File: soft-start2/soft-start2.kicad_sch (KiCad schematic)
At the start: 58 parts, among them J10 Conn_01x02_Pin, J11 Conn_01x02_Socket, J3 Conn_01x01_Pin, J4 Conn_01x01_Pin, J5 Conn_01x01_Pin, J8 Conn_01x01_Pin, K1 Relay_SPST-NO, K2 Relay_SPST-NO, M1 Motor_DC, Q1 IRFB3004PbF, Q2 IRFB3004PbF, SW1 SW_SPST_Temperature, U1 P0102BL, U2 TLC555xD, U3 TS391ILT, U4 IRS10752LPbF, U5 4011

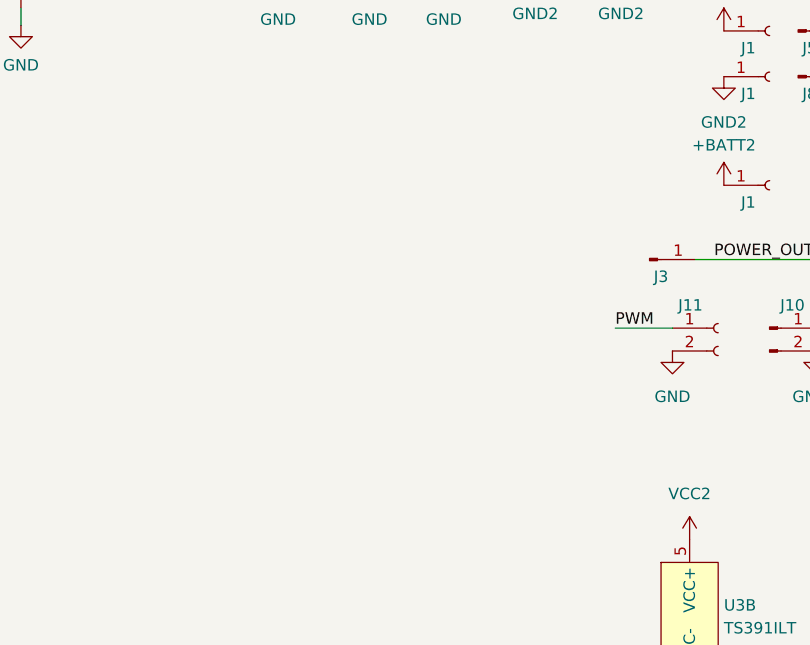
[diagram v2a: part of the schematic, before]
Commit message: [soft-start] Complete basic PCB for PWM soft-start
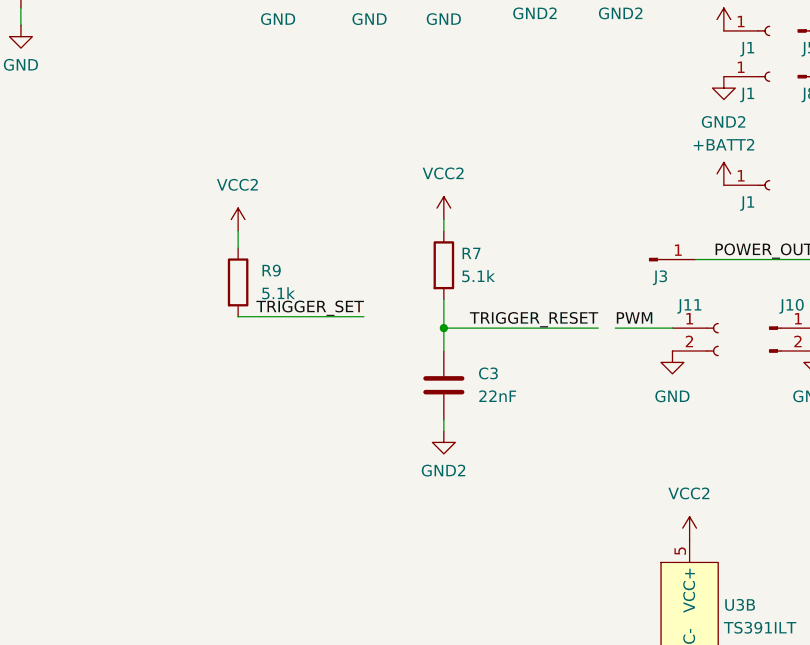
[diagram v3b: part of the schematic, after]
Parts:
- added C3: 22nF, Capacitor_THT:C_Disc_D5.0mm_W2.5mm_P5.00mm, symbol Device:C
- added R7: 5.1k, Resistor_THT:R_Axial_DIN0207_L6.3mm_D2.5mm_P7.62mm_Horizontal, symbol Device:R
- added R9: 5.1k, Resistor_THT:R_Axial_DIN0204_L3.6mm_D1.6mm_P5.08mm_Horizontal, symbol Device:R
- C2, C6: footprint Capacitor_THT:C_Disc_D6.0mm_W4.4mm_P5.00mm -> Capacitor_THT:C_Disc_D5.0mm_W2.5mm_P5.00mm
- C5: footprint Capacitor_THT:C_Disc_D5.0mm_W2.5mm_P5.00mm -> Capacitor_THT:C_Disc_D7.5mm_W5.0mm_P7.50mm
- R8: footprint Resistor_THT:R_Axial_DIN0207_L6.3mm_D2.5mm_P5.08mm_Vertical -> Resistor_THT:R_Axial_DIN0207_L6.3mm_D2.5mm_P10.16mm_Horizontal
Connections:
- net GND2: now also C3.2
- net TRIGGER_RESET: now also C3.1, R7.2
- net TRIGGER_SET: now also R9.2
- net VCC2: now also R7.1, R9.1
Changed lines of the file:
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@@
   (junction (at 140.335 173.355) (diameter 0) (color 0 0 0 0)
   )
+  (junction (at 236.855 67.945) (diameter 0) (color 0 0 0 0)
+  )
   (junction (at 67.31 62.23) (diameter 0) (color 0 0 0 0)
   )
@@
     (stroke (width 0) (type default))
   )
+  (wire (pts (xy 213.995 66.675) (xy 227.965 66.675))
+    (stroke (width 0) (type default))
+  )
   (wire (pts (xy 48.895 77.47) (xy 59.69 77.47))
     (stroke (width 0) (type default))
@@
     (stroke (width 0) (type default))
   )
+  (wire (pts (xy 236.855 67.945) (xy 254 67.945))
+    (stroke (width 0) (type default))
+  )
   (wire (pts (xy 17.145 87.63) (xy 24.13 87.63))
     (stroke (width 0) (type default))
@@
     (stroke (width 0) (type default))
   )
+  (wire (pts (xy 236.855 55.88) (xy 236.855 57.15))
+    (stroke (width 0) (type default))
+  )
   (wire (pts (xy 24.765 166.37) (xy 24.765 167.64))
     (stroke (width 0) (type default))
@@
     (stroke (width 0) (type default))
   )
+  (wire (pts (xy 236.855 67.945) (xy 236.855 70.485))
+    (stroke (width 0) (type default))
+  )
   (wire (pts (xy 24.765 149.225) (xy 30.48 149.225))
     (stroke (width 0) (type default))
@@
     (stroke (width 0) (type default))
   )
+  (wire (pts (xy 236.855 64.77) (xy 236.855 67.945))
+    (stroke (width 0) (type default))
+  )
   (wire (pts (xy 23.495 43.18) (xy 41.275 43.18))
     (stroke (width 0) (type default))
@@
     (stroke (width 0) (type default))
   )
+  (wire (pts (xy 213.995 57.15) (xy 213.995 59.055))
+    (stroke (width 0) (type default))
+  )
   (wire (pts (xy 150.495 62.23) (xy 164.465 62.23))
     (stroke (width 0) (type default))
@@
     (stroke (width 0) (type default))
   )
+  (wire (pts (xy 236.855 78.105) (xy 236.855 79.375))
+    (stroke (width 0) (type default))
+  )
   (wire (pts (xy 140.335 183.515) (xy 140.335 185.42))
     (stroke (width 0) (type default))
@@
     (effects (font (size 1.27 1.27)) (justify right bottom))
   )
+  (label "TRIGGER_SET" (at 227.965 66.675 180) (fields_autoplaced)
+    (effects (font (size 1.27 1.27)) (justify right bottom))
+  )
   (label "TRIGGER_OUT" (at 109.855 178.435 0) (fields_autoplaced)
     (effects (font (size 1.27 1.27)) (justify left bottom))
@@
     (effects (font (size 1.27 1.27)) (justify right bottom))
   )
+  (label "TRIGGER_RESET" (at 254 67.945 180) (fields_autoplaced)
+    (effects (font (size 1.27 1.27)) (justify right bottom))
+  )
   (symbol (lib_id "power:+BATT") (at 171.45 20.955 0) (unit 1)
     (in_bom yes) (on_board yes) (dnp no) (fields_autoplaced)
@@
     )
   )
+  (symbol (lib_id "Device:C") (at 236.855 74.295 0) (unit 1)
+    (in_bom yes) (on_board yes) (dnp no) (fields_autoplaced)
+    (property "Reference" "C3" (at 240.665 73.025 0)
+      (effects (font (size 1.27 1.27)) (justify left))
+    )
+    (property "Value" "22nF" (at 240.665 75.565 0)
+      (effects (font (size 1.27 1.27)) (justify left))
+    )
+    (property "Footprint" "Capacitor_THT:C_Disc_D5.0mm_W2.5mm_P5.00mm" (at 237.8202 78.105 0)
+      (effects (font (size 1.27 1.27)) hide)
+    )
+    (property "Datasheet" "~" (at 236.855 74.295 0)
+      (effects (font (size 1.27 1.27)) hide)
+    )
+    (pin "1")
+    (pin "2")
+    (instances
+      (project "soft-start"
+        (path "/dd3da890-32ef-4a5a-aea4-e5d2141f1ff1"
+          (reference "C3") (unit 1)
+        )
+      )
+      (project "soft-start2"
+        (path "/ebfa1560-6bfd-4c13-8584-dcc8e4637497"
+          (reference "C14") (unit 1)
+        )
+      )
+    )
+  )
   (symbol (lib_id "Device:R") (at 23.495 111.125 0) (unit 1)
     (in_bom yes) (on_board yes) (dnp no) (fields_autoplaced)
@@
       (effects (font (size 1.27 1.27)) (justify left))
     )
-    (property "Footprint" "Resistor_THT:R_Axial_DIN0207_L6.3mm_D2.5mm_P5.08mm_Vertical" (at 21.717 111.125 90)
+    (property "Footprint" "Resistor_THT:R_Axial_DIN0207_L6.3mm_D2.5mm_P10.16mm_Horizontal" (at 21.717 111.125 90)
       (effects (font (size 1.27 1.27)) hide)
     )
@@
     )
   )
+  (symbol (lib_id "Device:R") (at 236.855 60.96 0) (unit 1)
+    (in_bom yes) (on_board yes) (dnp no) (fields_autoplaced)
+    (property "Reference" "R7" (at 238.76 59.69 0)
+      (effects (font (size 1.27 1.27)) (justify left))
+    )
+    (property "Value" "5.1k" (at 238.76 62.23 0)
+      (effects (font (size 1.27 1.27)) (justify left))
+    )
+    (property "Footprint" "Resistor_THT:R_Axial_DIN0207_L6.3mm_D2.5mm_P7.62mm_Horizontal" (at 235.077 60.96 90)
+      (effects (font (size 1.27 1.27)) hide)
+    )
+    (property "Datasheet" "~" (at 236.855 60.96 0)
+      (effects (font (size 1.27 1.27)) hide)
+    )
+    (pin "1")
+    (pin "2")
+    (instances
+      (project "soft-start"
+        (path "/dd3da890-32ef-4a5a-aea4-e5d2141f1ff1"
+          (reference "R7") (unit 1)
+        )
+      )
+      (project "soft-start2"
+        (path "/ebfa1560-6bfd-4c13-8584-dcc8e4637497"
+          (reference "R10") (unit 1)
+        )
+      )
+    )
+  )
   (symbol (lib_id "power:GND2") (at 278.13 70.485 0) (unit 1)
     (in_bom yes) (on_board yes) (dnp no) (fields_autoplaced)
@@
     )
   )
+  (symbol (lib_id "vcc2:VCC2") (at 236.855 55.88 0) (unit 1)
+    (in_bom yes) (on_board yes) (dnp no) (fields_autoplaced)
+    (property "Reference" "#PWR053" (at 236.855 59.69 0)
+      (effects (font (size 1.27 1.27)) hide)
+    )
+    (property "Value" "VCC2" (at 236.855 50.8 0)
+      (effects (font (size 1.27 1.27)))
+    )
+    (property "Footprint" "" (at 236.855 55.88 0)
+      (effects (font (size 1.27 1.27)) hide)
+    )
+    (property "Datasheet" "" (at 236.855 55.88 0)
+      (effects (font (size 1.27 1.27)) hide)
+    )
+    (pin "1")
+    (instances
+      (project "soft-start2"
+        (path "/ebfa1560-6bfd-4c13-8584-dcc8e4637497"
+          (reference "#PWR053") (unit 1)
+        )
+      )
+    )
+  )
   (symbol (lib_id "Device:C") (at 118.745 50.8 0) (mirror y) (unit 1)
     (in_bom yes) (on_board yes) (dnp no) (fields_autoplaced)
@@
     )
   )
+  (symbol (lib_id "Device:R") (at 213.995 62.865 0) (unit 1)
+    (in_bom yes) (on_board yes) (dnp no) (fields_autoplaced)
+    (property "Reference" "R9" (at 216.535 61.595 0)
+      (effects (font (size 1.27 1.27)) (justify left))
+    )
+    (property "Value" "5.1k" (at 216.535 64.135 0)
+      (effects (font (size 1.27 1.27)) (justify left))
+    )
+    (property "Footprint" "Resistor_THT:R_Axial_DIN0204_L3.6mm_D1.6mm_P5.08mm_Horizontal" (at 212.217 62.865 90)
+      (effects (font (size 1.27 1.27)) hide)
+    )
+    (property "Datasheet" "~" (at 213.995 62.865 0)
+      (effects (font (size 1.27 1.27)) hide)
+    )
+    (pin "1")
+    (pin "2")
+    (instances
+      (project "soft-start"
+        (path "/dd3da890-32ef-4a5a-aea4-e5d2141f1ff1"
+          (reference "R9") (unit 1)
+        )
+      )
+      (project "soft-start2"
+        (path "/ebfa1560-6bfd-4c13-8584-dcc8e4637497"
+          (reference "R11") (unit 1)
+        )
+      )
+    )
+  )
   (symbol (lib_id "Device:C") (at 160.02 139.7 0) (unit 1)
     (in_bom yes) (on_board yes) (dnp no) (fields_autoplaced)
@@
       (effects (font (size 1.27 1.27)) (justify left))
     )
-    (property "Footprint" "Capacitor_THT:C_Disc_D6.0mm_W4.4mm_P5.00mm" (at 160.9852 143.51 0)
+    (property "Footprint" "Capacitor_THT:C_Disc_D5.0mm_W2.5mm_P5.00mm" (at 160.9852 143.51 0)
       (effects (font (size 1.27 1.27)) hide)
     )
@@
     )
   )
+  (symbol (lib_id "vcc2:VCC2") (at 213.995 57.15 0) (unit 1)
+    (in_bom yes) (on_board yes) (dnp no) (fields_autoplaced)
+    (property "Reference" "#PWR054" (at 213.995 60.96 0)
+      (effects (font (size 1.27 1.27)) hide)
+    )
+    (property "Value" "VCC2" (at 213.995 52.07 0)
+      (effects (font (size 1.27 1.27)))
+    )
+    (property "Footprint" "" (at 213.995 57.15 0)
+      (effects (font (size 1.27 1.27)) hide)
+    )
+    (property "Datasheet" "" (at 213.995 57.15 0)
+      (effects (font (size 1.27 1.27)) hide)
+    )
+    (pin "1")
+    (instances
+      (project "soft-start2"
+        (path "/ebfa1560-6bfd-4c13-8584-dcc8e4637497"
+          (reference "#PWR054") (unit 1)
+        )
+      )
+    )
+  )
   (symbol (lib_id "Device:C") (at 46.99 72.39 90) (unit 1)
     (in_bom yes) (on_board yes) (dnp no) (fields_autoplaced)
@@
       (effects (font (size 1.27 1.27)) (justify left))
     )
-    (property "Footprint" "Capacitor_THT:C_Disc_D6.0mm_W4.4mm_P5.00mm" (at 160.9852 116.84 0)
+    (property "Footprint" "Capacitor_THT:C_Disc_D5.0mm_W2.5mm_P5.00mm" (at 160.9852 116.84 0)
       (effects (font (size 1.27 1.27)) hide)
     )
@@
       (effects (font (size 1.27 1.27)) (justify left))
     )
-    (property "Footprint" "Capacitor_THT:C_Disc_D5.0mm_W2.5mm_P5.00mm" (at 257.5052 28.575 0)
+    (property "Footprint" "Capacitor_THT:C_Disc_D7.5mm_W5.0mm_P7.50mm" (at 257.5052 28.575 0)
       (effects (font (size 1.27 1.27)) hide)
     )
@@
         )
       )
+    )
+  )
+  (symbol (lib_id "power:GND2") (at 236.855 79.375 0) (unit 1)
+    (in_bom yes) (on_board yes) (dnp no) (fields_autoplaced)
+    (property "Reference" "#PWR052" (at 236.855 85.725 0)
+      (effects (font (size 1.27 1.27)) hide)
+    )
+    (property "Value" "GND2" (at 236.855 83.82 0)
+      (effects (font (size 1.27 1.27)))
+    )
+    (property "Footprint" "" (at 236.855 79.375 0)
+      (effects (font (size 1.27 1.27)) hide)
+    )
+    (property "Datasheet" "" (at 236.855 79.375 0)
+      (effects (font (size 1.27 1.27)) hide)
+    )
+    (pin "1")
+    (instances
+      (project "soft-start2"
+        (path "/ebfa1560-6bfd-4c13-8584-dcc8e4637497"
+          (reference "#PWR052") (unit 1)
+        )
+      )

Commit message: [soft-start] Reset PWM generator on trigger latch. Update plot settings
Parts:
- added J12: Conn_01x01_Pin, Connector_Wire:SolderWire-0.5sqmm_1x01_D0.9mm_OD2.1mm, symbol Connector:Conn_01x01_Pin
- added J13: Conn_01x01_Socket, Connector_Wire:SolderWire-0.5sqmm_1x01_D0.9mm_OD2.1mm, symbol Connector:Conn_01x01_Socket
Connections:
- net VCC: no longer U2.4 (R)
- net TRIGGER_OUT_INV: now reaches C2.1, Rt2.1, U1.12
- net TRIGGER_OUT_INV: now also J12.1 (Pin_1)
- new net: J13.1 (Pin_1), U2.4 (R)
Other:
- note added: "Connections: J12 -> J13 J11 -> J10 J5 -> J6 J7 -> J8 J3 - controlled cooling fan J1 - external battery +12V J2 - external GND J9 - external battery +12V L1 is an external relay capable of driving M1's full power current (approx. 30 amps)"
- note removed: "L1 is an external relay capable of driving M1's full power current (approx. 30 amps)"
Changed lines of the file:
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@@
   (junction (at 153.67 135.89) (diameter 0) (color 0 0 0 0)
   )
+  (junction (at 160.02 135.89) (diameter 0) (color 0 0 0 0)
+  )
   (junction (at 142.875 173.355) (diameter 0) (color 0 0 0 0)
   )
@@
     (stroke (width 0) (type default))
   )
-  (wire (pts (xy 23.495 43.18) (xy 41.275 43.18))
-    (stroke (width 0) (type default))
-  )
   (wire (pts (xy 167.005 83.82) (xy 179.705 83.82))
     (stroke (width 0) (type default))
@@
     (stroke (width 0) (type default))
   )
+  (wire (pts (xy 31.75 43.18) (xy 41.275 43.18))
+    (stroke (width 0) (type default))
+  )
   (wire (pts (xy 66.675 38.1) (xy 75.565 38.1))
     (stroke (width 0) (type default))
@@
     (stroke (width 0) (type default))
   )
+  (wire (pts (xy 160.02 135.89) (xy 171.45 135.89))
+    (stroke (width 0) (type default))
+  )
   (wire (pts (xy 29.845 60.96) (xy 33.655 60.96))
     (stroke (width 0) (type default))
@@
     (effects (font (size 1.27 1.27)) (justify left bottom))
   )
-  (text "L1 is an external relay capable of driving M1's full power current (approx. 30 amps)\n"
+  (text "Connections:\nJ12 -> J13\nJ11 -> J10\nJ5 -> J6\nJ7 -> J8\n\nJ3 - controlled cooling fan\nJ1 - external battery +12V\nJ2 - external GND\nJ9 - external battery +12V\n\nL1 is an external relay capable of driving M1's full power current (approx. 30 amps)"
     (at 182.88 162.56 0)
     (effects (font (size 1.27 1.27)) (justify left bottom))
@@
     (effects (font (size 1.27 1.27)) (justify right bottom))
   )
+  (label "TRIGGER_OUT_INV" (at 171.45 135.89 180) (fields_autoplaced)
+    (effects (font (size 1.27 1.27)) (justify right bottom))
+  )
   (label "PWM2" (at 283.21 67.945 180) (fields_autoplaced)
     (effects (font (size 1.27 1.27)) (justify right bottom))
@@
     )
   )
-  (symbol (lib_id "power:VCC") (at 23.495 43.18 0) (unit 1)
-    (in_bom yes) (on_board yes) (dnp no) (fields_autoplaced)
-    (property "Reference" "#PWR018" (at 23.495 46.99 0)
-      (effects (font (size 1.27 1.27)) hide)
-    )
-    (property "Value" "VCC" (at 23.495 38.1 0)
-      (effects (font (size 1.27 1.27)))
-    )
-    (property "Footprint" "" (at 23.495 43.18 0)
-      (effects (font (size 1.27 1.27)) hide)
-    )
-    (property "Datasheet" "" (at 23.495 43.18 0)
-      (effects (font (size 1.27 1.27)) hide)
-    )
-    (pin "1")
-    (instances
-      (project "soft-start2"
-        (path "/ebfa1560-6bfd-4c13-8584-dcc8e4637497"
-          (reference "#PWR018") (unit 1)
-        )
-      )
-    )
-  )
   (symbol (lib_id "vcc2:VCC2") (at 267.97 34.925 0) (unit 1)
     (in_bom yes) (on_board yes) (dnp no) (fields_autoplaced)
@@
     )
   )
+  (symbol (lib_id "Connector:Conn_01x01_Pin") (at 176.53 135.89 180) (unit 1)
+    (in_bom yes) (on_board yes) (dnp no) (fields_autoplaced)
+    (property "Reference" "J12" (at 175.895 130.81 0)
+      (effects (font (size 1.27 1.27)))
+    )
+    (property "Value" "Conn_01x01_Pin" (at 175.895 133.35 0)
+      (effects (font (size 1.27 1.27)) hide)
+    )
+    (property "Footprint" "Connector_Wire:SolderWire-0.5sqmm_1x01_D0.9mm_OD2.1mm" (at 176.53 135.89 0)
+      (effects (font (size 1.27 1.27)) hide)
+    )
+    (property "Datasheet" "~" (at 176.53 135.89 0)
+      (effects (font (size 1.27 1.27)) hide)
+    )
+    (pin "1")
+    (instances
+      (project "soft-start2"
+        (path "/ebfa1560-6bfd-4c13-8584-dcc8e4637497"
+          (reference "J12") (unit 1)
+        )
+      )
+    )
+  )
   (symbol (lib_id "power:GND") (at 53.975 48.26 0) (unit 1)
     (in_bom yes) (on_board yes) (dnp no) (fields_autoplaced)
@@
         )
       )
+    )
+  )
+  (symbol (lib_id "Connector:Conn_01x01_Socket") (at 26.67 43.18 180) (unit 1)
+    (in_bom yes) (on_board yes) (dnp no) (fields_autoplaced)
+    (property "Reference" "J13" (at 27.305 38.1 0)
+      (effects (font (size 1.27 1.27)))
+    )
+    (property "Value" "Conn_01x01_Socket" (at 27.305 40.64 0)
+      (effects (font (size 1.27 1.27)) hide)
+    )
+    (property "Footprint" "Connector_Wire:SolderWire-0.5sqmm_1x01_D0.9mm_OD2.1mm" (at 26.67 43.18 0)
+      (effects (font (size 1.27 1.27)) hide)
+    )
+    (property "Datasheet" "~" (at 26.67 43.18 0)
+      (effects (font (size 1.27 1.27)) hide)
+    )
+    (pin "1")
+    (instances
+      (project "soft-start2"
+        (path "/ebfa1560-6bfd-4c13-8584-dcc8e4637497"
+          (reference "J13") (unit 1)
+        )
+      )

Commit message: [soft-start] Add capacitor discharge resistor. It limits capacitor voltage to approx. 90% of VCC
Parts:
- added R12: 24k, Resistor_THT:R_Axial_DIN0207_L6.3mm_D2.5mm_P7.62mm_Horizontal, symbol Device:R
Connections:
- net GND: now also R12.2
- net U1_CONT: now also R12.1
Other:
- moved on the sheet: J12
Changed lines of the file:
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@@
   (junction (at 150.495 62.23) (diameter 0) (color 0 0 0 0)
   )
+  (junction (at 164.465 53.34) (diameter 0) (color 0 0 0 0)
+  )
   (junction (at 140.335 160.02) (diameter 0) (color 0 0 0 0)
   )
@@
   )
   (junction (at 160.02 135.89) (diameter 0) (color 0 0 0 0)
+  )
+  (junction (at 164.465 62.23) (diameter 0) (color 0 0 0 0)
   )
   (junction (at 142.875 173.355) (diameter 0) (color 0 0 0 0)
@@
     (stroke (width 0) (type default))
   )
+  (wire (pts (xy 180.975 62.23) (xy 180.975 61.595))
+    (stroke (width 0) (type default))
+  )
   (wire (pts (xy 150.495 22.86) (xy 150.495 26.035))
     (stroke (width 0) (type default))
@@
     (stroke (width 0) (type default))
   )
+  (wire (pts (xy 153.67 151.765) (xy 153.67 135.89))
+    (stroke (width 0) (type default))
+  )
   (wire (pts (xy 140.335 185.42) (xy 140.335 189.23))
     (stroke (width 0) (type default))
@@
     (stroke (width 0) (type default))
   )
+  (wire (pts (xy 164.465 62.23) (xy 180.975 62.23))
+    (stroke (width 0) (type default))
+  )
   (wire (pts (xy 67.945 109.22) (xy 69.85 109.22))
     (stroke (width 0) (type default))
@@
     (stroke (width 0) (type default))
   )
+  (wire (pts (xy 180.975 53.34) (xy 164.465 53.34))
+    (stroke (width 0) (type default))
+  )
   (wire (pts (xy 189.865 32.385) (xy 189.865 34.29))
     (stroke (width 0) (type default))
@@
     (stroke (width 0) (type default))
   )
+  (wire (pts (xy 156.845 151.765) (xy 153.67 151.765))
+    (stroke (width 0) (type default))
+  )
   (wire (pts (xy 135.89 53.34) (xy 150.495 53.34))
     (stroke (width 0) (type default))
@@
   )
   (wire (pts (xy 24.765 167.64) (xy 42.545 167.64))
+    (stroke (width 0) (type default))
+  )
+  (wire (pts (xy 180.975 53.975) (xy 180.975 53.34))
     (stroke (width 0) (type default))
   )
@@
     )
   )
+  (symbol (lib_id "Device:R") (at 180.975 57.785 0) (mirror y) (unit 1)
+    (in_bom yes) (on_board yes) (dnp no) (fields_autoplaced)
+    (property "Reference" "R12" (at 179.07 56.515 0)
+      (effects (font (size 1.27 1.27)) (justify left))
+    )
+    (property "Value" "24k" (at 179.07 59.055 0)
+      (effects (font (size 1.27 1.27)) (justify left))
+    )
+    (property "Footprint" "Resistor_THT:R_Axial_DIN0207_L6.3mm_D2.5mm_P7.62mm_Horizontal" (at 182.753 57.785 90)
+      (effects (font (size 1.27 1.27)) hide)
+    )
+    (property "Datasheet" "~" (at 180.975 57.785 0)
+      (effects (font (size 1.27 1.27)) hide)
+    )
+    (pin "1")
+    (pin "2")
+    (instances
+      (project "soft-start2"
+        (path "/ebfa1560-6bfd-4c13-8584-dcc8e4637497"
+          (reference "R12") (unit 1)
+        )
+      )
+    )
+  )
   (symbol (lib_id "Device:R_Potentiometer_Trim") (at 23.495 121.92 0) (unit 1)
     (in_bom yes) (on_board yes) (dnp no) (fields_autoplaced)
@@
     )
   )
-  (symbol (lib_id "Connector:Conn_01x01_Pin") (at 176.53 135.89 180) (unit 1)
-    (in_bom yes) (on_board yes) (dnp no) (fields_autoplaced)
-    (property "Reference" "J12" (at 175.895 130.81 0)
-      (effects (font (size 1.27 1.27)))
-    )
-    (property "Value" "Conn_01x01_Pin" (at 175.895 133.35 0)
-      (effects (font (size 1.27 1.27)) hide)
-    )
-    (property "Footprint" "Connector_Wire:SolderWire-0.5sqmm_1x01_D0.9mm_OD2.1mm" (at 176.53 135.89 0)
-      (effects (font (size 1.27 1.27)) hide)
-    )
-    (property "Datasheet" "~" (at 176.53 135.89 0)
-      (effects (font (size 1.27 1.27)) hide)
-    )
+  (symbol (lib_id "Connector:Conn_01x01_Pin") (at 161.925 151.765 180) (unit 1)
+    (in_bom yes) (on_board yes) (dnp no)
+    (property "Reference" "J12" (at 164.465 151.765 0)
+      (effects (font (size 1.27 1.27)))
+    )
+    (property "Value" "Conn_01x01_Pin" (at 161.29 149.225 0)
+      (effects (font (size 1.27 1.27)) hide)
+    )
+    (property "Footprint" "Connector_Wire:SolderWire-0.5sqmm_1x01_D0.9mm_OD2.1mm" (at 161.925 151.765 0)
+      (effects (font (size 1.27 1.27)) hide)
+    )
+    (property "Datasheet" "~" (at 161.925 151.765 0)
+      (effects (font (size 1.27 1.27)) hide)
+    )
